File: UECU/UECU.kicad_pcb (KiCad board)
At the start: 2 copper layers, 17 parts, among them J1 Conn_pwr, J2 Conn_display, J3 Conn_acc, U1 ESP32-DevKitC, U2 LM2596_buck

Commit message: add front layer
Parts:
- removed H5, H6: 3.7, MountingHole:MountingHole_3.7mm
- added C10: 10uF, Capacitor_THT:C_Disc_D5.0mm_W2.5mm_P5.00mm, F.Cu at (79.2, 53.8)
- added C11: 100nF, Capacitor_THT:C_Disc_D5.0mm_W2.5mm_P5.00mm, F.Cu at (81.8, 53.8)
- added C12: 10uF, Capacitor_THT:C_Disc_D5.0mm_W2.5mm_P5.00mm, F.Cu at (141.5, 71.6)
- added C13: 100nF, Capacitor_THT:C_Disc_D5.0mm_W2.5mm_P5.00mm, F.Cu at (141.5, 74.8)
- added C14: 10uF, Capacitor_THT:C_Disc_D5.0mm_W2.5mm_P5.00mm, F.Cu at (48.7, 65.2)
- added C15: 100nF, Capacitor_THT:C_Disc_D5.0mm_W2.5mm_P5.00mm, F.Cu at (48.7, 72.9)
- added C3: 10pF, Capacitor_THT:C_Disc_D5.0mm_W2.5mm_P5.00mm, F.Cu at (83.1, 85.6)
- added C4: 10pF, Capacitor_THT:C_Disc_D5.0mm_W2.5mm_P5.00mm, F.Cu at (71.6, 85.6)
- added C5: 10pF, Capacitor_THT:C_Disc_D5.0mm_W2.5mm_P5.00mm, F.Cu at (57.6, 79.2)
- added C6: 10uF, Capacitor_THT:C_Disc_D5.0mm_W2.5mm_P5.00mm, F.Cu at (89.3, 97.6)
- added C7: 100nF, Capacitor_THT:C_Disc_D5.0mm_W2.5mm_P5.00mm, F.Cu at (85.5, 97.6)
- added C8: 10uF, Capacitor_THT:C_Disc_D5.0mm_W2.5mm_P5.00mm, F.Cu at (137.6, 60.1)
- added C9: 100nF, Capacitor_THT:C_Disc_D5.0mm_W2.5mm_P5.00mm, F.Cu at (137.6, 67.7)
- added D2: 1N4007, Diode_THT:D_A-405_P7.62mm_Horizontal, F.Cu at (50.0, 90.6)
- added D3: ZENER 3V3, Diode_THT:D_A-405_P7.62mm_Horizontal, F.Cu at (57.6, 83.0)
- added MCU1: ESP32-DevKitC, Espressif:ESP32-DevKitC, F.Cu at (138.9, 74.1)
- added P1: LM2596_buck, StepDown:StepDown_LM2596, F.Cu at (133.8, 67.8)
- added R4: 2k2, Resistor_THT:R_Axial_DIN0207_L6.3mm_D2.5mm_P7.62mm_Horizontal, F.Cu at (75.4, 62.7)
- added R5: 10k, Resistor_THT:R_Axial_DIN0207_L6.3mm_D2.5mm_P7.62mm_Horizontal, F.Cu at (83.0, 70.3)
- added R6: 59k, Resistor_THT:R_Axial_DIN0207_L6.3mm_D2.5mm_P7.62mm_Horizontal, F.Cu at (50.0, 86.8)
- added R7: 2k, Resistor_THT:R_Axial_DIN0207_L6.3mm_D2.5mm_P7.62mm_Horizontal, F.Cu at (70.3, 89.4)
- added R8: 10k, Resistor_THT:R_Axial_DIN0207_L6.3mm_D2.5mm_P7.62mm_Horizontal, F.Cu at (67.8, 77.9)
- added R9: 10k, Resistor_THT:R_Axial_DIN0207_L6.3mm_D2.5mm_P7.62mm_Horizontal, F.Cu at (75.4, 66.5)
- added S1: ~, Connector_PinHeader_2.54mm:PinHeader_1x08_P2.54mm_Vertical, F.Cu at (81.8, 50.0)
- added T1: LoRa-SX1276, LoRa_SX1276:LoRa_SX1276, F.Cu at (59.9, 64.0)
- added U3: 4N25, Package_DIP:DIP-6_W7.62mm, F.Cu at (71.6, 81.8)
- J3: value Conn_acc -> Conn_SENSORS; footprint Connector_JST:JST_XH_B4B-XH-A_1x04_P2.50mm_Vertical -> Connector_JST:JST_XH_B3B-XH-A_1x03_P2.50mm_Vertical
- R1, R3: footprint Resistor_THT:R_Axial_DIN0204_L3.6mm_D1.6mm_P5.08mm_Horizontal -> Resistor_THT:R_Axial_DIN0207_L6.3mm_D2.5mm_P7.62mm_Horizontal
- R2: value 2k2 -> 2k; footprint Resistor_THT:R_Axial_DIN0204_L3.6mm_D1.6mm_P5.08mm_Horizontal -> Resistor_THT:R_Axial_DIN0207_L6.3mm_D2.5mm_P7.62mm_Horizontal
- U1: value ESP32-DevKitC -> 4N25; footprint Espressif:ESP32-DevKitC -> Package_DIP:DIP-6_W7.62mm
- U2: value LM2596_buck -> 4N25; footprint StepDown:StepDown_LM2596 -> Package_DIP:DIP-6_W7.62mm
- moved J3 111.8 mm to (65.2, 97.5), turned to 180 degrees
- moved H1 110.9 mm to (50.0, 50.0)
- moved H3 110.0 mm to (50.0, 98.3)
- moved C2 107.5 mm to (89.3, 64.0), turned to -90 degrees
- moved R1 104.4 mm to (83.0, 58.9), turned to 180 degrees
- moved J2 96.5 mm to (80.4, 97.5), turned to 180 degrees
- moved R2 95.7 mm to (81.8, 89.4)
- moved U2 89.5 mm to (61.4, 89.4), turned to 90 degrees
- moved C1 80.9 mm to (89.4, 58.9), turned to 180 degrees
- moved J1 65.2 mm to (143.3, 60.2), turned to 90 degrees
- moved R3 63.2 mm to (128.7, 71.6)
- moved H2 55.3 mm to (144.0, 50.0)
- moved D1 48.0 mm to (145.2, 66.5), turned to 180 degrees
- moved U1 36.5 mm to (83.0, 81.7), turned to 90 degrees
- moved H4 17.3 mm to (144.0, 98.3)
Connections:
- D1 pad 1: Net-(D1-K) -> GND
- D1 pad 2: LED_ALIVE -> Net-(D1-A)
- J2 pad 2: TXD2 -> RXD2
- J2 pad 3: RXD2 -> TXD2
- J3 pad 1: +5V -> CONN_EMG
- J3 pad 2: SCL -> CONN_SPD
- J3 pad 3: SDA -> CONN_RPM
- R2 pad 1: VBAT-3V -> CONN_EMG
- R2 pad 2: GND -> Net-(C3-Pad1)
- R3 pad 1: Net-(D1-K) -> LED_ALIVE
- R3 pad 2: GND -> Net-(D1-A)
- U1 pad 1: +3V3 -> Net-(C3-Pad1)
- U1 pad 2: unconnected-(U1-EN-Pad2) -> GND
- U1 pad 4: unconnected-(U1-GPIO39/SENSOR_VN/ADC1_CH3-Pad4) -> SIGNAL_EMG
- U1 pad 5: unconnected-(U1-GPIO34/VDET_1/ADC1_CH6-Pad5) -> +3V3
- U1 pad 6: VBAT-3V -> unconnected-(U1-Pad6)
- U2 pad 1: +12V -> Net-(D3-K)
- U2 pad 3: GND -> unconnected-(U2-NC-Pad3)
- U2 pad 4: +5V -> SIGNAL_RPM
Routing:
- net +12V: track 0.00 -> 74.4 mm, vias 0 -> 1
- net +5V: track 0.00 -> 68.9 mm
- net TXD2: track 0.00 -> 43.6 mm
- net RXD2: track 0.00 -> 37.2 mm
- net CONN_EMG: track 0.00 -> 22.3 mm
- net LED_ALIVE: track 0.00 -> 21.9 mm
- net +3V3: track 0.00 -> 20.2 mm
- net CONN_SPD: track 0.00 -> 13.5 mm
- net Net-(D3-K): track 0.00 -> 13.2 mm
- net Net-(C4-Pad1): track 0.00 -> 11.7 mm
- net Net-(C3-Pad1): track 0.00 -> 11.7 mm
- net SIGNAL_SPD: track 0.00 -> 10.5 mm
- net Net-(D1-A): track 0.00 -> 8.45 mm
- net CONN_RPM: track 0.00 -> 7.93 mm
- net SIGNAL_EMG: track 0.00 -> 7.40 mm
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- added copper zone on B.Cu, net GND
- added copper zone on F.Cu, net GND
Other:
- board outline added: 101.2 x 55.4 mm

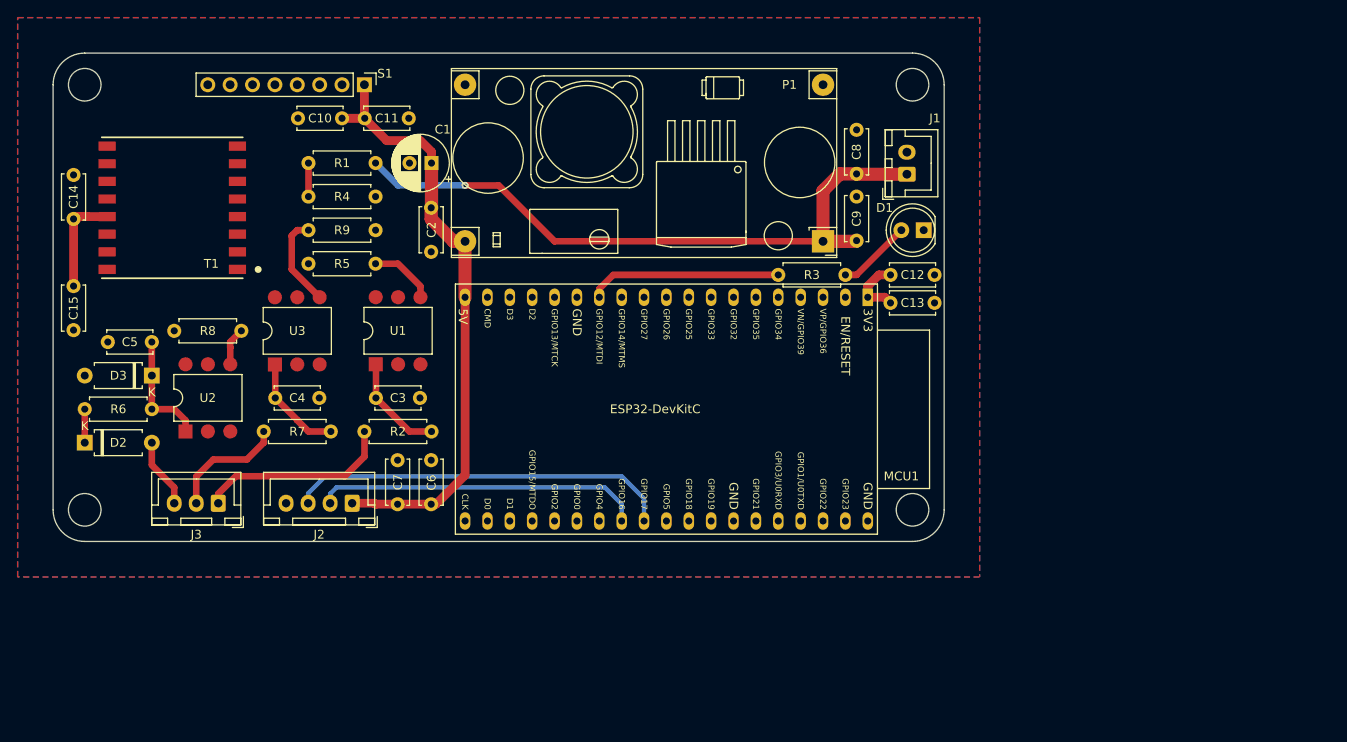
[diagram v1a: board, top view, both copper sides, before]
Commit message: finish bottom layer
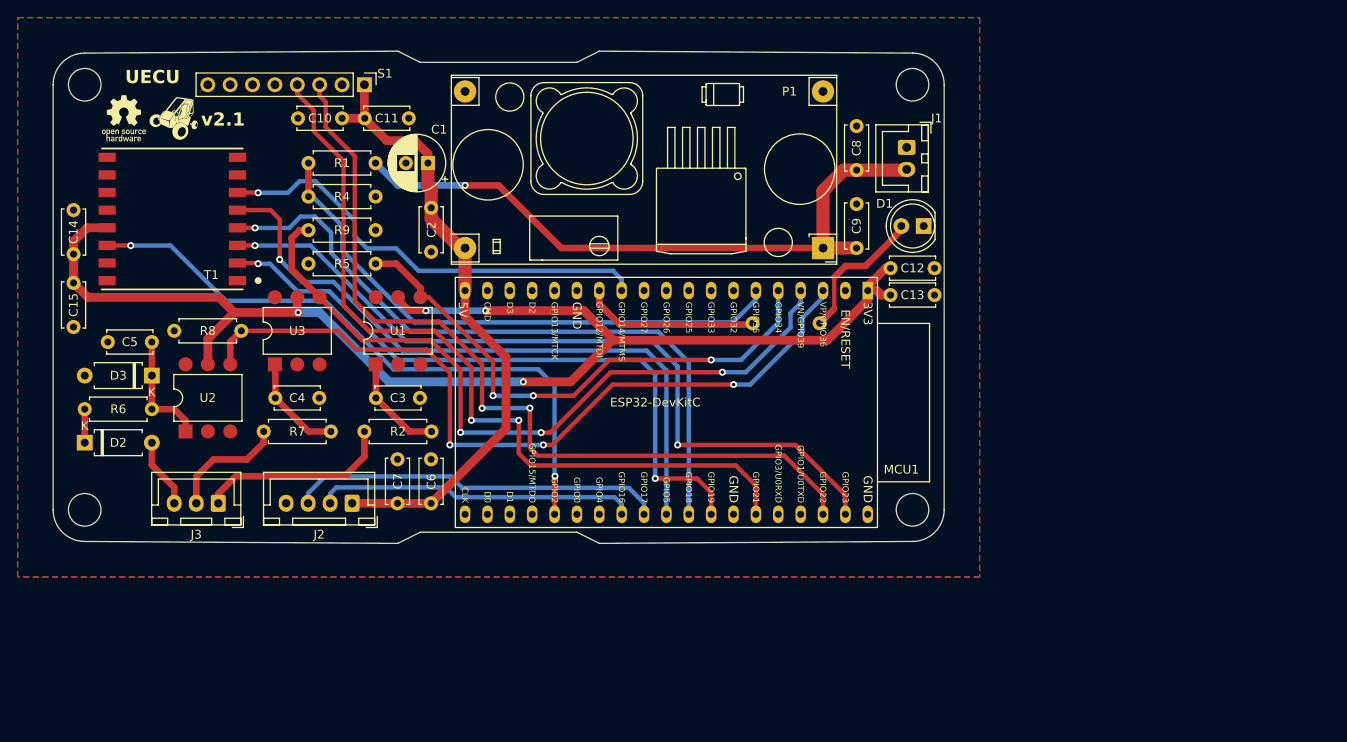
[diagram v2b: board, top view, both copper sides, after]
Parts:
- added G***: LOGO, LOGO, F.Cu at (54.4, 53.8)
- added G***: LOGO, LOGO, F.Cu at (60.2, 53.8)
- R3: moved to B.Cu
- moved R3 6.22 mm to (125.8, 77.1)
- moved C14 3.99 mm to (48.7, 69.2)
- moved J1 3.05 mm to (143.3, 57.1), turned to -90 degrees
- moved T1 1.27 mm to (59.9, 65.2)
- moved C13 0.89 mm to (141.5, 73.9)
- moved C9 0.84 mm to (137.6, 68.5)
- moved C12 0.76 mm to (141.5, 70.8)
- moved MCU1 0.76 mm to (138.9, 73.4)
- moved P1 0.76 mm to (133.8, 68.5)
- moved D1 0.47 mm to (145.2, 66.0)
- moved C8 0.43 mm to (137.6, 59.7)
- moved C1 0.41 mm to (89.0, 58.9)
- moved C15 0.36 mm to (48.7, 72.5)
- moved C6 0.10 mm to (89.3, 97.5)
- moved C7 0.10 mm to (85.5, 97.5)
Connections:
- J1 pad 1: +12V -> GND
- J1 pad 2: GND -> +12V
- MCU1 pad 3: SIGNAL_SPD -> SIGNAL_RPM
- MCU1 pad 4: SIGNAL_RPM -> SIGNAL_SPD
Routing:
- net +3V3: track 20.2 -> 151.1 mm, vias 0 -> 4
- net SCL: track 0.00 -> 96.3 mm, vias 0 -> 2
- net SDA: track 0.00 -> 91.5 mm, vias 0 -> 2
- net MOSI: track 0.00 -> 88.2 mm, vias 0 -> 2
- net SIGNAL_RPM: track 4.33 -> 89.2 mm, vias 0 -> 3
- net SCK: track 0.00 -> 77.2 mm, vias 0 -> 1
- net NSS: track 0.00 -> 75.3 mm, vias 0 -> 1
- net MISO: track 0.00 -> 74.0 mm, vias 0 -> 2
- net SIGNAL_SPD: track 10.5 -> 83.9 mm, vias 0 -> 3
- net DIO: track 0.00 -> 72.0 mm, vias 0 -> 2
- net VBAT-3V: track 3.81 -> 64.2 mm
- net SIGNAL_EMG: track 7.40 -> 61.9 mm, vias 0 -> 3
- net RST: track 0.00 -> 51.1 mm, vias 0 -> 1
- net Net-(D1-A): track 8.45 -> 16.2 mm
- net +5V: track 68.9 -> 71.5 mm
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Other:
- board size 101.2 x 55.4 mm -> 101.2 x 55.9 mm
- board text added: "UECU"
- board text added: "v2.1"

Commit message: add ground vias
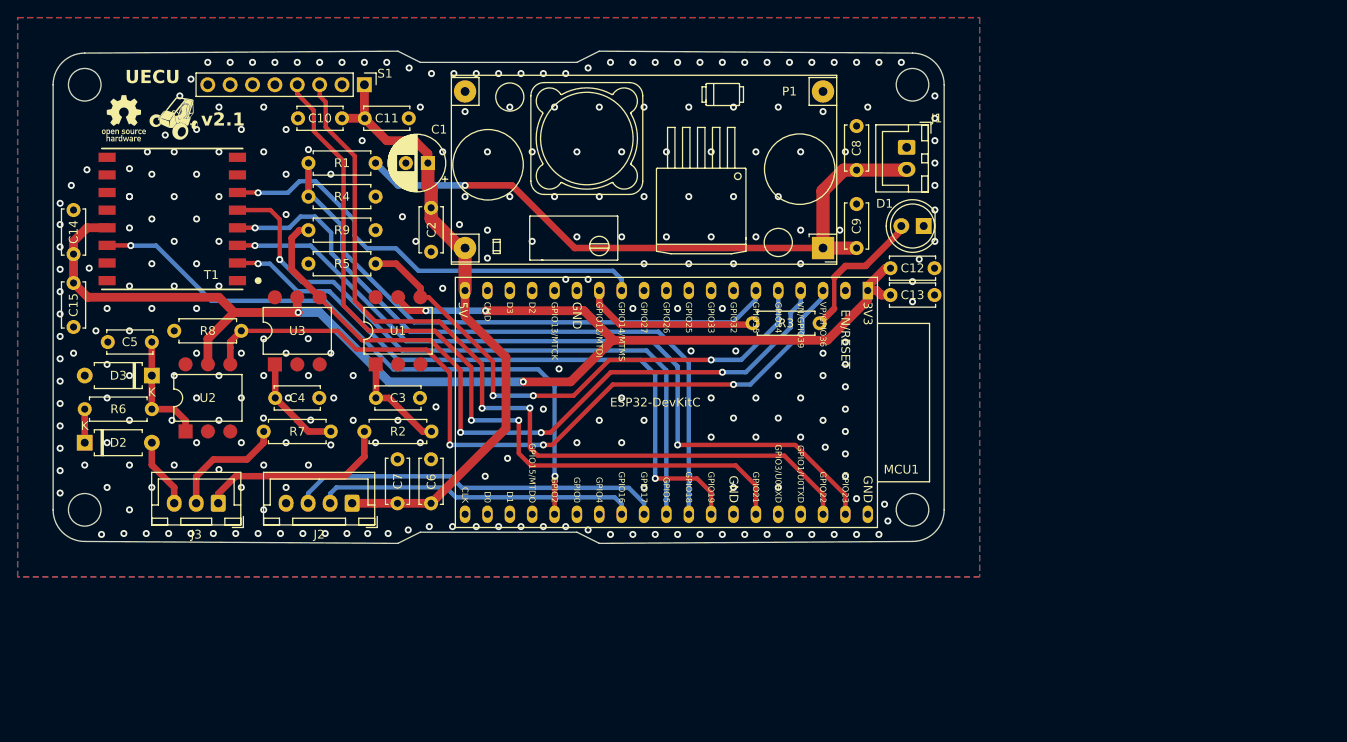
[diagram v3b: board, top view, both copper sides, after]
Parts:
- R3: moved to F.Cu
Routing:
- net GND: vias 0 -> 270

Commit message: create new module
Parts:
- removed G*** (x2): LOGO, LOGO
- added L1: ~, Logos:parahybaja, F.Cu at (60.2, 53.8)
- added L2: ~, Logos:open_hardware, F.Cu at (54.4, 53.6)
- added REF**: TestPoint_Pad_D1.5mm, TestPoint:TestPoint_Pad_D1.5mm, F.Cu at (89.6, 71.4)
- added REF**: TestPoint_Pad_D1.5mm, TestPoint:TestPoint_Pad_D1.5mm, F.Cu at (69.1, 81.7)
- added REF**: TestPoint_Pad_D1.5mm, TestPoint:TestPoint_Pad_D1.5mm, F.Cu at (139.9, 52.6)
- added REF**: TestPoint_Pad_D1.5mm, TestPoint:TestPoint_Pad_D1.5mm, F.Cu at (72.8, 62.4)
- added REF**: TestPoint_Pad_D1.5mm, TestPoint:TestPoint_Pad_D1.5mm, F.Cu at (68.0, 92.9)
- added REF**: TestPoint_Pad_D1.5mm, TestPoint:TestPoint_Pad_D1.5mm, F.Cu at (77.7, 72.1)
- added REF**: TestPoint_Pad_D1.5mm, TestPoint:TestPoint_Pad_D1.5mm, F.Cu at (86.3, 65.5)
- added REF**: TestPoint_Pad_D1.5mm, TestPoint:TestPoint_Pad_D1.5mm, F.Cu at (57.8, 92.9)
- added REFe: TestPoint_Pad_D1.5mm, TestPoint:TestPoint_Pad_D1.5mm, F.Cu at (62.7, 92.9)
- moved C14 0.69 mm to (49.4, 69.2)
- moved C15 0.66 mm to (49.4, 72.5)
- moved C12 0.65 mm to (140.8, 70.8)
- moved C13 0.65 mm to (140.8, 73.9)
- moved D1 0.61 mm to (144.6, 66.0)
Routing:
- net +12V: track 75.6 -> 82.7 mm
- net SIGNAL_EMG: track 61.9 -> 65.2 mm
- net +5V: track 71.5 -> 74.6 mm
- net VBAT-3V: track 64.2 -> 67.0 mm
- net SIGNAL_RPM: track 89.2 -> 91.8 mm
- net SIGNAL_SPD: track 83.9 -> 86.4 mm
- net +3V3: track 151.1 -> 148.9 mm
- net CONN_EMG: track 22.3 -> 23.9 mm
- net GND: vias 270 -> 268
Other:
- board size 101.2 x 55.9 mm -> 99.8 x 55.9 mm
- board text added: "WayWayWay"
- board text added: "v2.4"
- board text removed: "v2.1"
